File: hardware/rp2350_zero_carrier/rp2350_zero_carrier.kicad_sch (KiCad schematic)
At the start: 17 parts, among them J1 RP2350-Zero_Header(23pin,GPIO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, J2 USB-A_Host(Neltron_5075AR-04-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, J3 RP2350-Zero_Header(23pin,ボード2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, SW1 1回路2接点スイッチ(3pin,NKK_115643,ON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, SW2 1回路2接点スイッチ(3pin,NKK_115643,ON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, SW3 1回路2接点スイッチ(3pin,NKK_115643,ON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, SW4 1回路2接点スイッチ(3pin,NKK_115643,ON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, SW5 1回路2接点スイッチ(3pin,NKK_115643,ON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, SW6 タクトスイッチ4pin(Akizuki_DTS-63-N-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, U1 TPS2553DBVR

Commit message: Implement fail-latched USB power redesign
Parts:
- added COUT_HF: 100nF X7R 50V, rp2350_zero_carrier:C_0603, symbol Device:C
- added R_EN: 100k EN pulldown, rp2350_zero_carrier:R_0603, symbol Device:R
- J1: value RP2350-Zero_Header(23pin,GPIO20+電源3,確定済み-右列/下段は要目視確認) -> RP2350_Zero_Header_23p; symbol Connector_Generic:Conn_01x20 -> rp2350_zero_carrier:RP2350_Zero_Header_23p
- J2: value USB-A_Host(Neltron_5075AR-04-WH,VBUS/D-/D+/GND) -> USB_A_Neltron_5075AR-04-WH; symbol Connector_Generic:Conn_01x04 -> rp2350_zero_carrier:USB_A_6PIN
- J3: value RP2350-Zero_Header(23pin,ボード2役割=UART_mirror受信,GP5のみ使用) -> RP2350_Zero_Header_23p; symbol Connector_Generic:Conn_01x20 -> rp2350_zero_carrier:RP2350_Zero_Header_23p
- SW1: value 1回路2接点スイッチ(3pin,NKK_115643,ON-OFF用途;Mute/GP28) -> SW_SPDT_NKK_115643_Slide
- SW2: value 1回路2接点スイッチ(3pin,NKK_115643,ON-OFF用途;Filter/GP29) -> SW_SPDT_NKK_115643_Slide
- SW3: value 1回路2接点スイッチ(3pin,NKK_115643,ON-OFF用途;予備/GP27,ファーム未対応) -> SW_SPDT_NKK_115643_Slide
- SW4: value 1回路2接点スイッチ(3pin,NKK_115643,ON-OFF用途;USB-A_VBUS電源スイッチ) -> SW_SPDT_NKK_115643_Slide
- SW5: value 1回路2接点スイッチ(3pin,NKK_115643,ON-OFF用途;サステイン/J3のGP29,issue#8) -> SW_SPDT_NKK_115643_Slide
- SW6: value タクトスイッチ4pin(Akizuki_DTS-63-N-V-BLK;リセット/J3のGP28,issue#6;pin1/2=GND束ね,pin3/4=GP28束ね) -> SW_TACT_Akizuki_DTS63
- U1: symbol TPS2553DBVR -> rp2350_zero_carrier:TPS2553DBVR
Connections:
- net GND: now also J1.2 (Pin_2), J2.5 (SHIELD), J2.6 (SHIELD), J3.2 (Pin_2), SW1.3, SW2.3, SW3.3, SW5.3, SW6.1 (Pin_1), SW6.2 (Pin_2), COUT_HF.2, R_EN.2; no longer J1.19 (Pin_19), J3.19 (Pin_19), SW6.3 (Pin_3), SW6.4 (Pin_4)
- net GP0_UART0_TX: now also J1.10 (Pin_10); no longer J1.11 (Pin_11)
- net GP12_USB_DP: now also J1.20 (Pin_20); no longer J1.2 (Pin_2)
- net GP13_USB_DM: now also J1.19 (Pin_19); no longer J1.3 (Pin_3), J2.3 (Pin_3), R1.2
- net GP1_UART0_RX: now also J1.11 (Pin_11); no longer J1.10 (Pin_10)
- net GP27_SW3_SPARE: now also J1.6 (Pin_6), SW3.2; no longer J1.15 (Pin_15)
- net GP28_SW1_GAME_MODE: now also J1.5 (Pin_5), SW1.2; no longer J1.16 (Pin_16)
- net GP28_SW6_RESET: now also J3.5 (Pin_5), SW6.3 (Pin_3), SW6.4 (Pin_4); no longer J3.16 (Pin_16), SW6.1 (Pin_1), SW6.2 (Pin_2)
- net GP29_SW2_LYRE_MODE: now also J1.4 (Pin_4), SW2.2; no longer J1.17 (Pin_17)
- net GP29_SW5_SUSTAIN: now also J3.4 (Pin_4), SW5.2; no longer J3.17 (Pin_17)
- net J3_GP0_UART0_TX: now also J3.10 (Pin_10); no longer J3.11 (Pin_11)
- net J3_GP1_UART0_RX: now also J3.11 (Pin_11); no longer J3.10 (Pin_10)
- net UART_MIRROR: now also J1.14 (Pin_14), J3.15 (Pin_15); no longer J1.7 (Pin_7), J3.6 (Pin_6)
- net UART_MIRROR_RETURN: now also J1.15 (Pin_15), J3.14 (Pin_14); no longer J1.6 (Pin_6), J3.7 (Pin_7)
- net USB_PWR_FAULT_N: now also J1.22 (Pin_22)
- net VBUS_5V: now also J1.1 (Pin_1); no longer J1.20 (Pin_20)
- net VBUS_TPS_IN: no longer R_FAULT.1, U1.3 (EN)
- net VBUS_USB_A: now also SW4.2, COUT_HF.1
- net VBUS_USB_A_SW: now also SW4.3
- new net 3V3: J1.3 (Pin_3), R_FAULT.1
- new net USB_A_DP: J2.3 (D+), R1.2
- new net USB_PWR_EN: J1.23 (Pin_23), R_EN.1, U1.3 (EN)
- no-connect marks 0 -> 30
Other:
- note added: "U1 TPS2553DBVR: EN(pin3)=USB_PWR_EN/GP9、FAULT(pin4)=USB_PWR_FAULT_N/GP10。 R_EN=100kΩでboot default off。FAULTはR_FAULT=100kΩで3V3へpull-up。 OUT(pin6)=VBUS_USB_A、COUT_HF=100nFをOUT-GND直近に配置。"
- note removed: "U1(TPS2553DBVR)ピン配置に関する注記: EN(pin3)はIN(pin1)と同じネットVBUS_TPS_INに意図的に直結している(TPS2553はEN=Highでオンのため、常時ON固定の設計)。 OUT(pin6)のネット名はVBUS_USB_Aであり、文字列に"OUT"を含まない。 ICのピン名はデータシート(SLVS841F)準拠でIN/GND/EN/FAULT/ILIM/OUTの6本固定であり、ここに現れるネット名(VBUS_TPS_IN等)とは別物。照合はネット名ではなくピン名で行うこと。"
- moved on the sheet: R1, R2, SW1, SW2, SW3

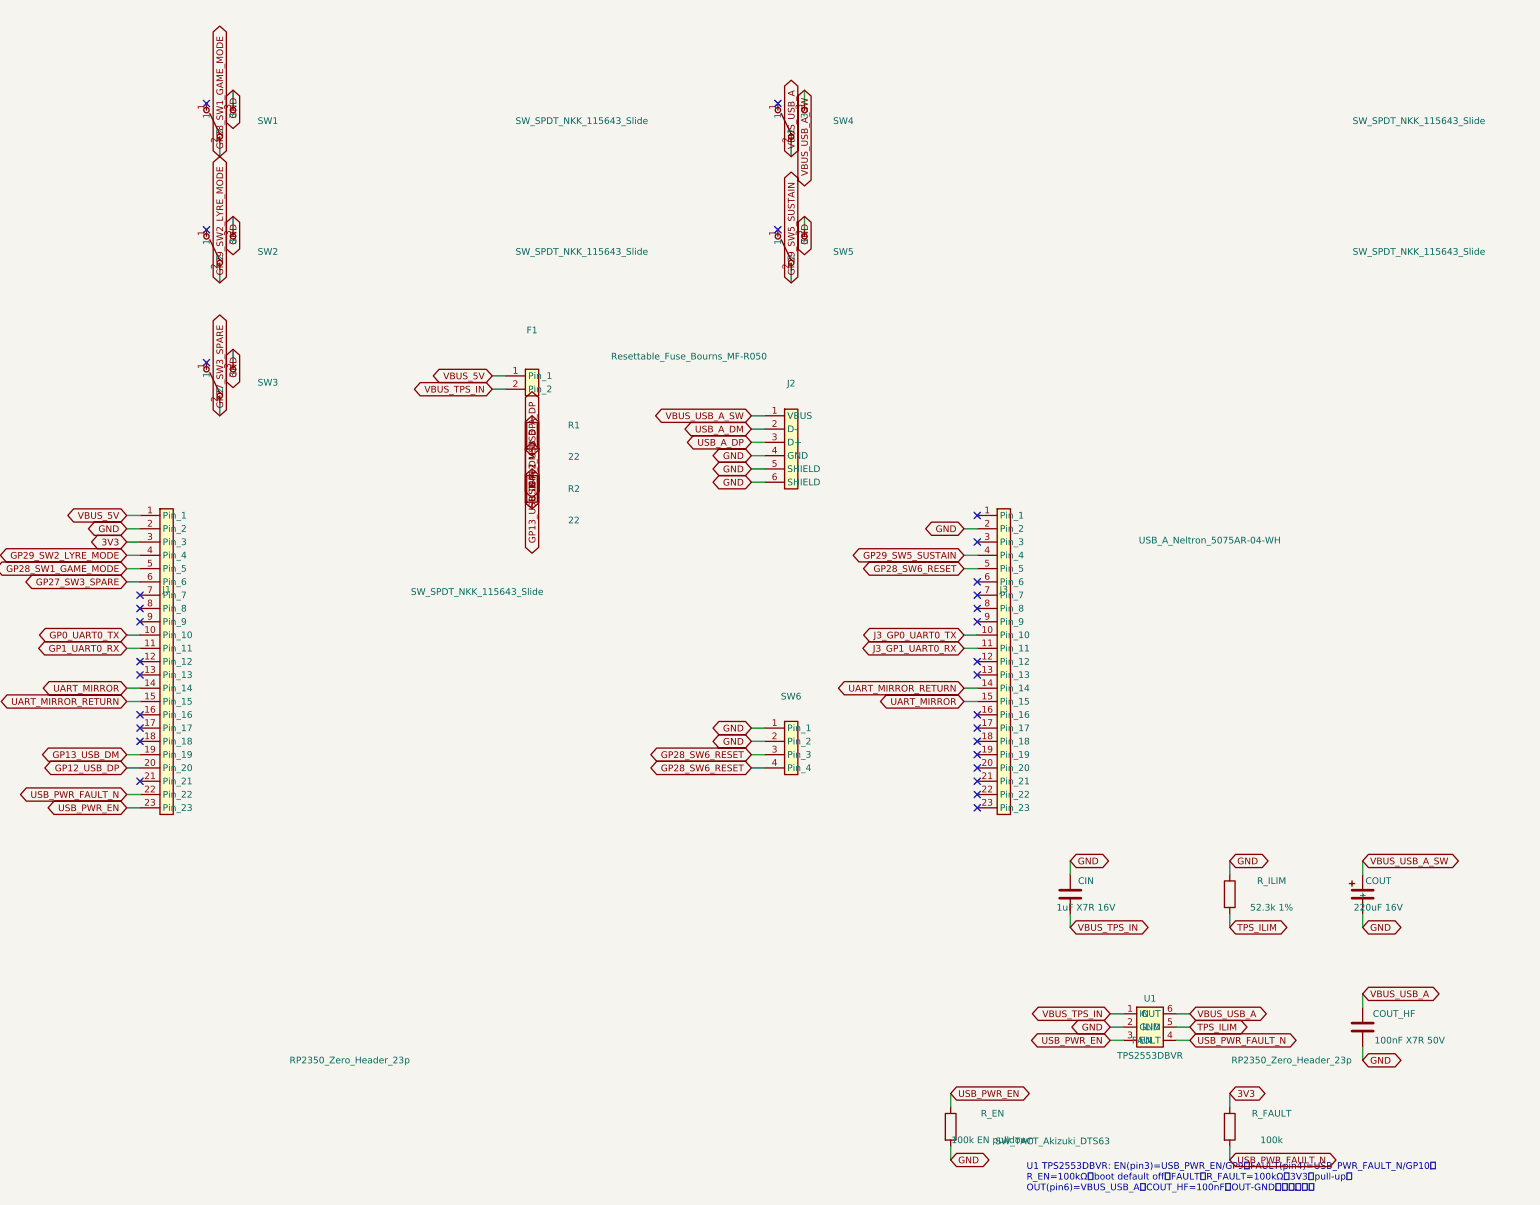
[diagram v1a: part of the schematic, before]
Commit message: Fix PCB annotations and manufacturing gates
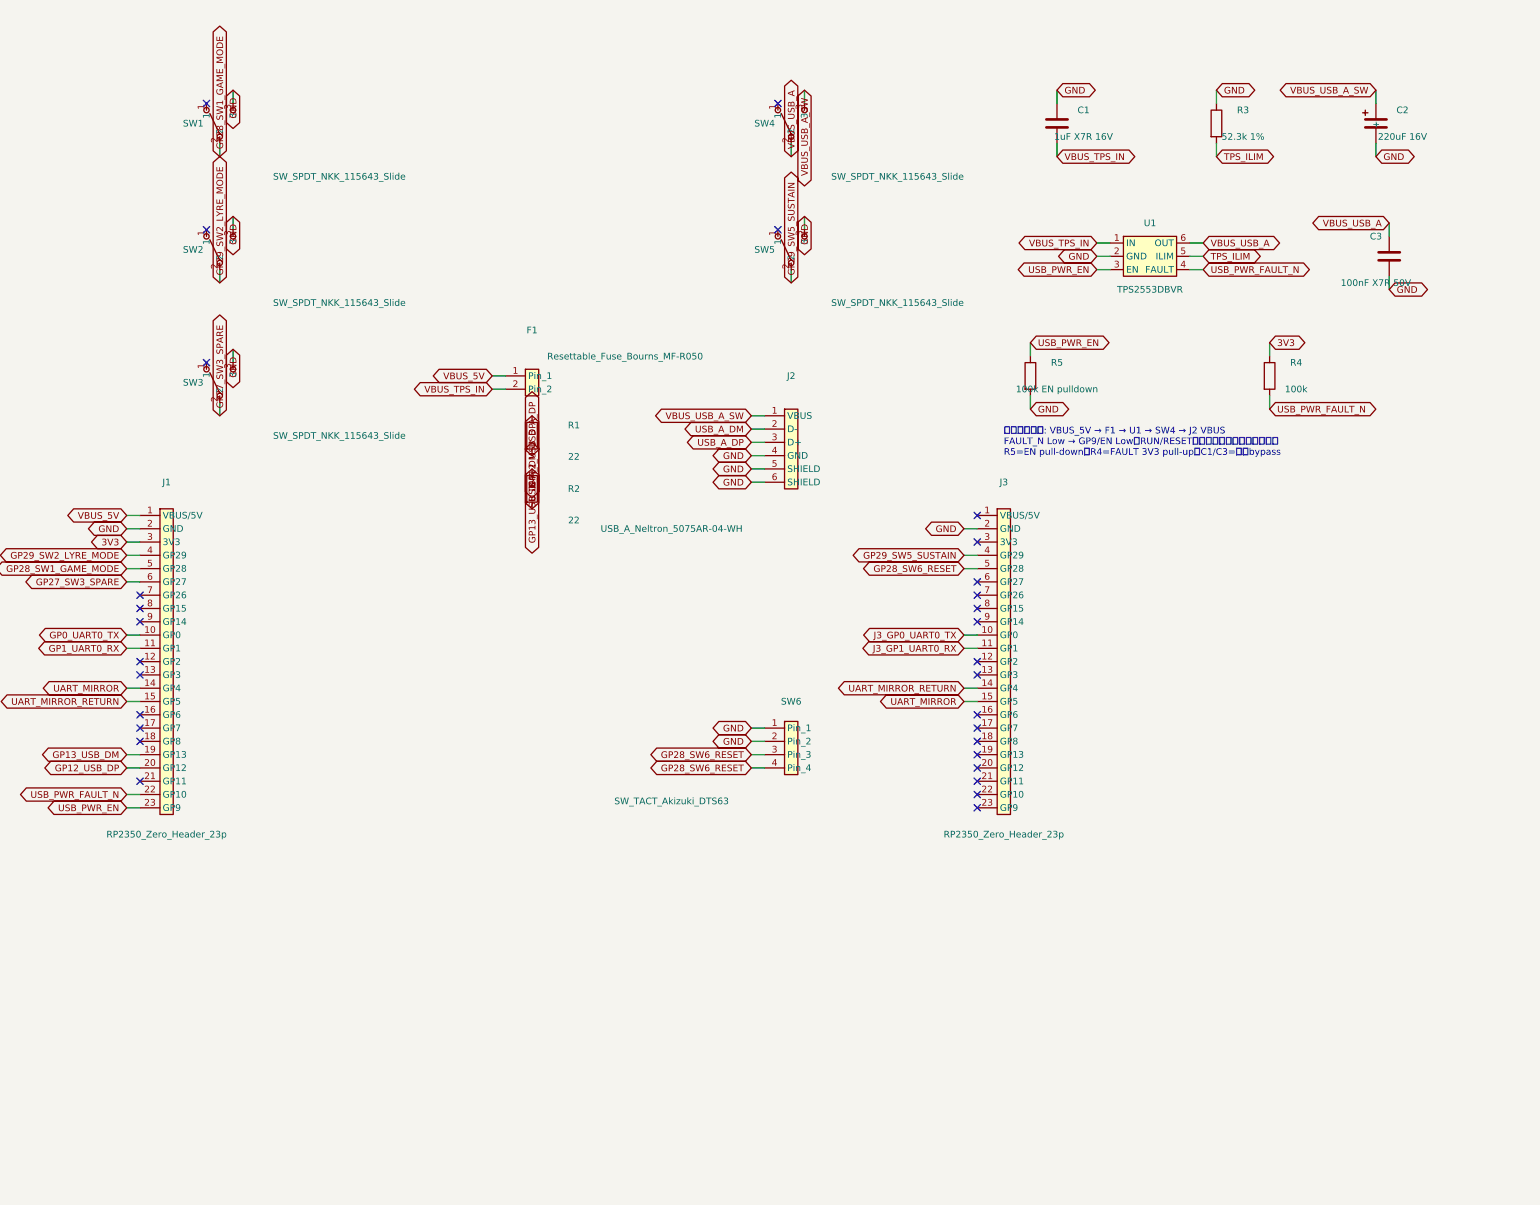
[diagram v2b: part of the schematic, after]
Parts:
- renumbered CIN to C1, COUT to C2, COUT_HF to C3, R_ILIM to R3, R_FAULT to R4, R_EN to R5
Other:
- note added: "電源ブロック: VBUS_5V → F1 → U1 → SW4 → J2 VBUS FAULT_N Low → GP9/EN Low（RUN/RESETまたは電源再投入まで保持） R5=EN pull-down、R4=FAULT 3V3 pull-up、C1/C3=局所bypass"
- note removed: "U1 TPS2553DBVR: EN(pin3)=USB_PWR_EN/GP9、FAULT(pin4)=USB_PWR_FAULT_N/GP10。 R_EN=100kΩでboot default off。FAULTはR_FAULT=100kΩで3V3へpull-up。 OUT(pin6)=VBUS_USB_A、COUT_HF=100nFをOUT-GND直近に配置。"
- moved on the sheet: C1, C2, C3, J1, J3, R3, R4, R5, U1
